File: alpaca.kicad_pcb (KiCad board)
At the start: 2 copper layers, 130 x 51 mm, 84 parts, among them P1 Debug, P2 Endpoint, U1 Raspberry_Pico, U10 ST_LSM6, U12 ST_LSM6, U2 Alpsalpine_RKJXV, U3 Alpsalpine_EC10E, U4 Alpsalpine_RKJXM, U6 NXP_PCAL6416A, U8 NXP_PCAL6416A

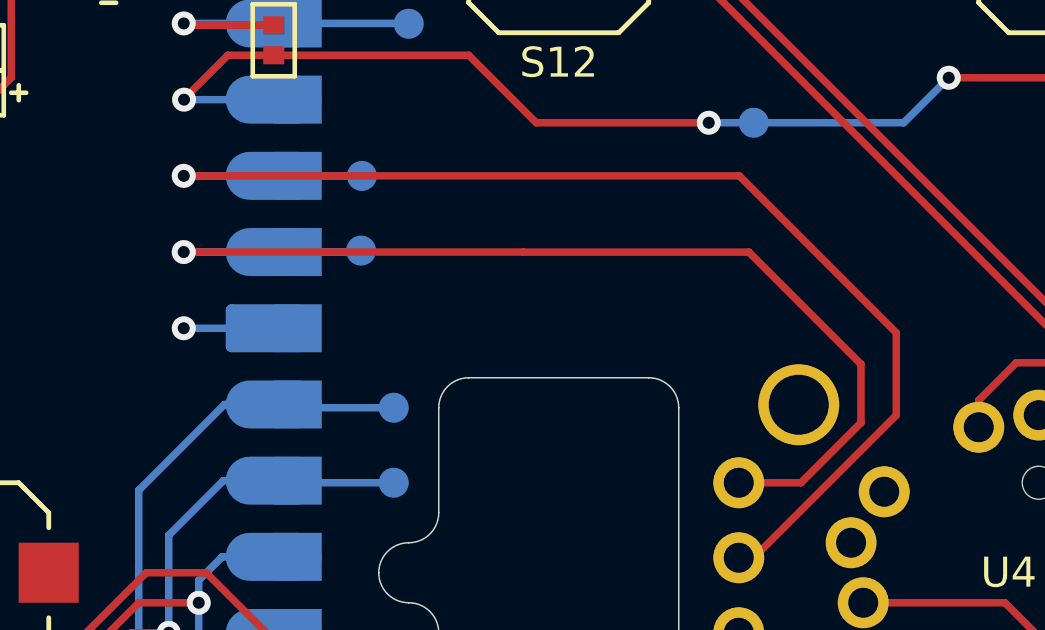
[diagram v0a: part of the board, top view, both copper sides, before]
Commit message: Adding hierarchical sheets and bus definitions
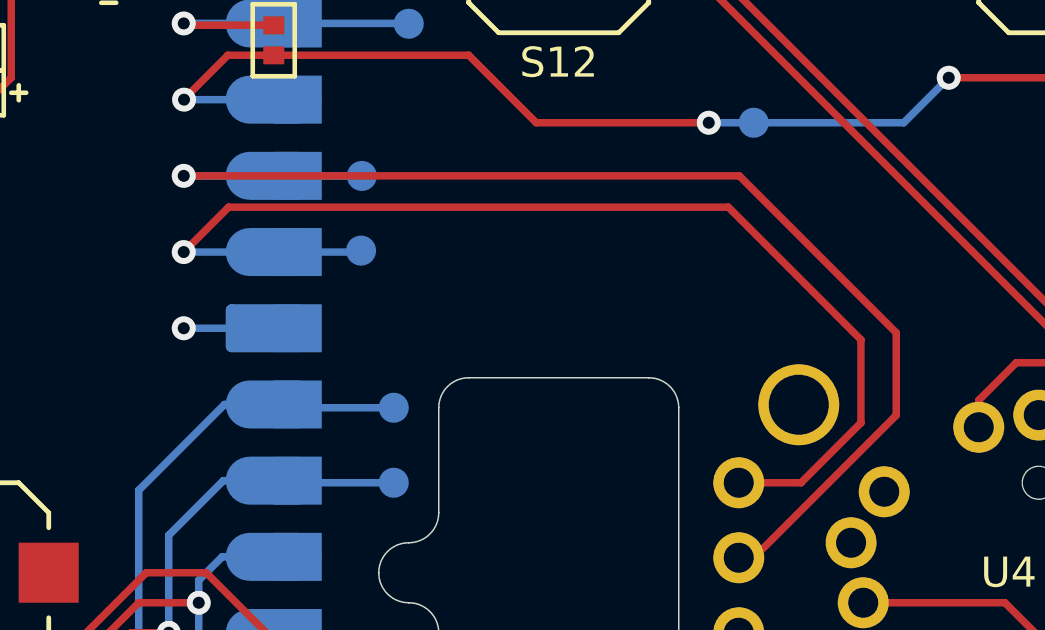
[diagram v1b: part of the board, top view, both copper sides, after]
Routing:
- net GP9: track 36.9 -> 38.6 mm
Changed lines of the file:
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@@
   (segment (start 111.3 61.77) (end 113.4336 61.77) (width 0.25) (layer "B.Cu") (net 17))
   (segment (start 113.4336 61.77) (end 113.4364 61.7728) (width 0.25) (layer "B.Cu") (net 17))
+  (segment (start 130.0734 67.2338) (end 130.0734 70.0024) (width 0.25) (layer "F.Cu") (net 18))
+  (segment (start 107.5 64.31) (end 108.9958 62.8142) (width 0.25) (layer "F.Cu") (net 18))
+  (segment (start 108.9958 62.8142) (end 125.6538 62.8142) (width 0.25) (layer "F.Cu") (net 18))
+  (segment (start 130.0734 70.0024) (end 128.0758 72) (width 0.25) (layer "F.Cu") (net 18))
+  (segment (start 125.6538 62.8142) (end 130.0734 67.2338) (width 0.25) (layer "F.Cu") (net 18))
   (segment (start 128.0758 72) (end 126 72) (width 0.25) (layer "F.Cu") (net 18))
-  (segment (start 130.0734 70.0024) (end 128.0758 72) (width 0.25) (layer "F.Cu") (net 18))
-  (segment (start 107.5 64.31) (end 118.8212 64.31) (width 0.25) (layer "F.Cu") (net 18))
-  (segment (start 118.837 64.3128) (end 126.3396 64.3128) (width 0.25) (layer "F.Cu") (net 18))
-  (segment (start 126.3396 64.3128) (end 130.0734 68.0466) (width 0.25) (layer "F.Cu") (net 18))
-  (segment (start 130.0734 68.0466) (end 130.0734 70.0024) (width 0.25) (layer "F.Cu") (net 18))
   (via (at 107.5 64.31) (size 0.8) (drill 0.4) (layers "F.Cu" "B.Cu") (net 18))
   (segment (start 113.363 64.31) (end 113.411 64.262) (width 0.25) (layer "B.Cu") (net 18))
@@
     (connect_pads (clearance 0.4))
     (min_thickness 0.2) (filled_areas_thickness no)
-    (fill (thermal_gap 0.4) (thermal_bridge_width 0.4))
+    (fill yes (thermal_gap 0.4) (thermal_bridge_width 0.4))
     (polygon
       (pts
@@
     (connect_pads (clearance 0.4))
     (min_thickness 0.2) (filled_areas_thickness no)
-    (fill (thermal_gap 0.4) (thermal_bridge_width 0.4))
+    (fill yes (thermal_gap 0.4) (thermal_bridge_width 0.4))
     (polygon
       (pts
@@
     (connect_pads (clearance 0.4))
     (min_thickness 0.2) (filled_areas_thickness no)
-    (fill (thermal_gap 0.4) (thermal_bridge_width 0.4))
+    (fill yes (thermal_gap 0.4) (thermal_bridge_width 0.4))
     (polygon
       (pts
@@
     (connect_pads (clearance 0.4))
     (min_thickness 0.2) (filled_areas_thickness no)
-    (fill (thermal_gap 0.4) (thermal_bridge_width 0.4))
-    (polygon
-      (pts
+    (fill yes (thermal_gap 0.4) (thermal_bridge_width 0.4))
+    (polygon
+      (pts
